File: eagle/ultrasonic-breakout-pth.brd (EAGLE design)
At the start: 54.9 x 41.9 mm, 25 parts, among them Q1 16 MHz, U1 ATMEGA328P_PDIP

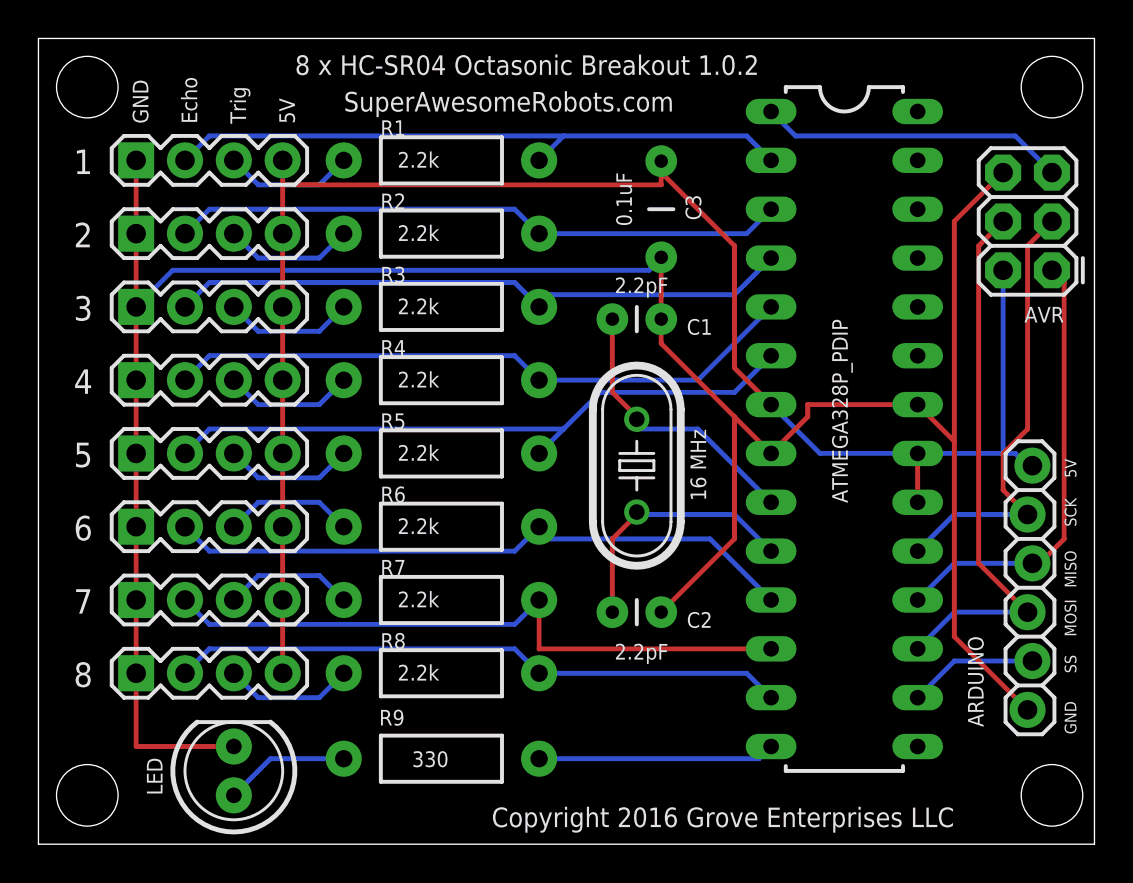
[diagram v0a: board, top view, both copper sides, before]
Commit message: update board to use locking molex connectors
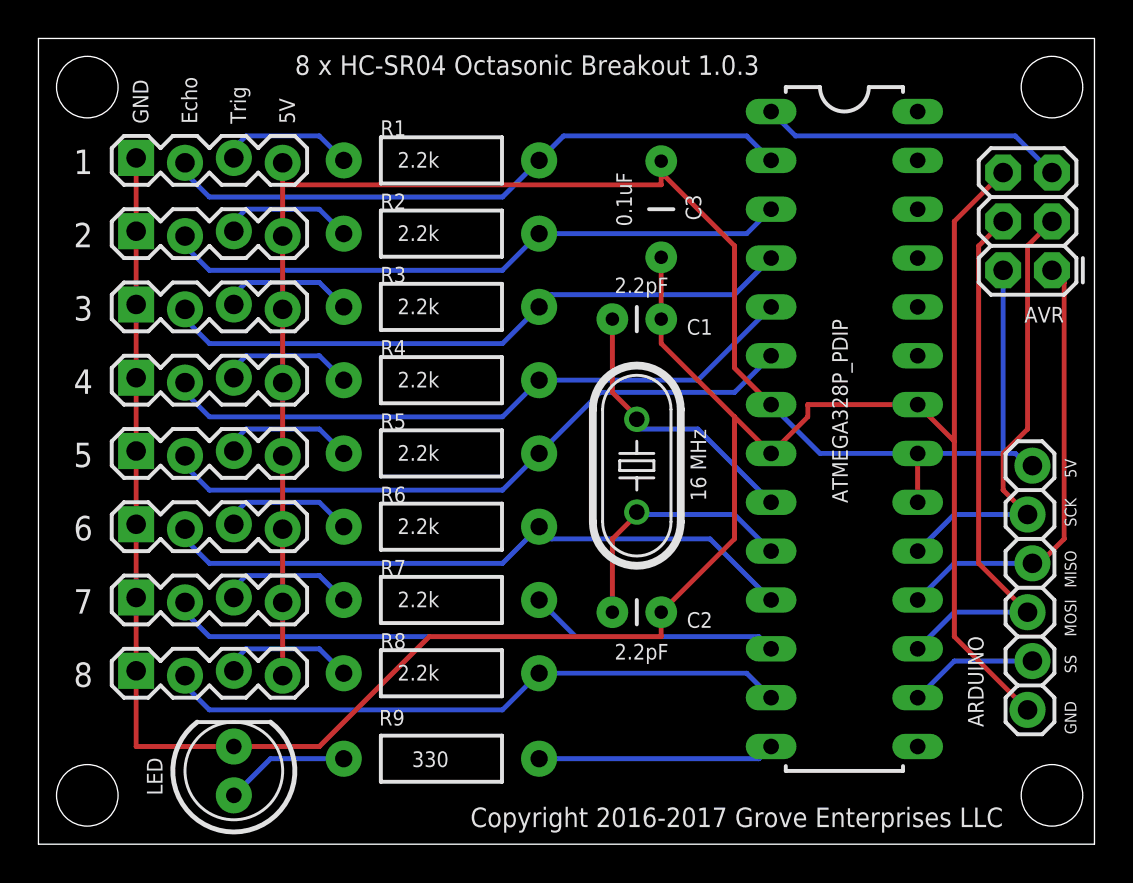
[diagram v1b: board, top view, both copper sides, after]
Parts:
- 1, 2, 3, 4, 5, 6, 7, 8: device SparkFun-Connectors:1X04 -> SparkFun-Connectors:1X04_LOCK
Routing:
- net GND: track 130.6 -> 128.2 mm
- net PD7: track 32.1 -> 32.8 mm
- net PD5: track 33.1 -> 33.9 mm
- net PD2: track 32.6 -> 33.4 mm
- net PD3: track 33.1 -> 33.9 mm
- net PD1: track 32.1 -> 32.8 mm
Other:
- board text added: "8 x HC-SR04 Octasonic Breakout 1.0.3"
- board text added: "Copyright 2016-2017 Grove Enterprises LLC"
- board text removed: "8 x HC-SR04 Octasonic Breakout 1.0.2"
- board text removed: "Copyright 2016 Grove Enterprises LLC"
- board text removed: "SuperAwesomeRobots.com"
